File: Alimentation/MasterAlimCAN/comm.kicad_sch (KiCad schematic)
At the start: 17 parts, among them J2 DEBUG, J3 In App Prog, J4 I2C1_5, J5 I2C2_5, J6 CAN1, J7 CAN2, SW1 RESET, SW2 BOOT0, U6 MCP2558FD-xSN

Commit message: Init placement for MasterAlimCAN
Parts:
- J3: footprint Connector_JST:JST_EH_S2B-EH_1x02_P2.50mm_Horizontal -> Connector_JST:JST_PH_S2B-PH-K_1x02_P2.00mm_Horizontal
- J4, J5, J6, J7: footprint Connector_JST:JST_EH_S4B-EH_1x04_P2.50mm_Horizontal -> Connector_JST:JST_PH_S4B-PH-K_1x04_P2.00mm_Horizontal
- renumbered C16 to C15, C17 to C16, C18 to C17, R11 to R10, R12 to R11, R13 to R12, U6 to U5

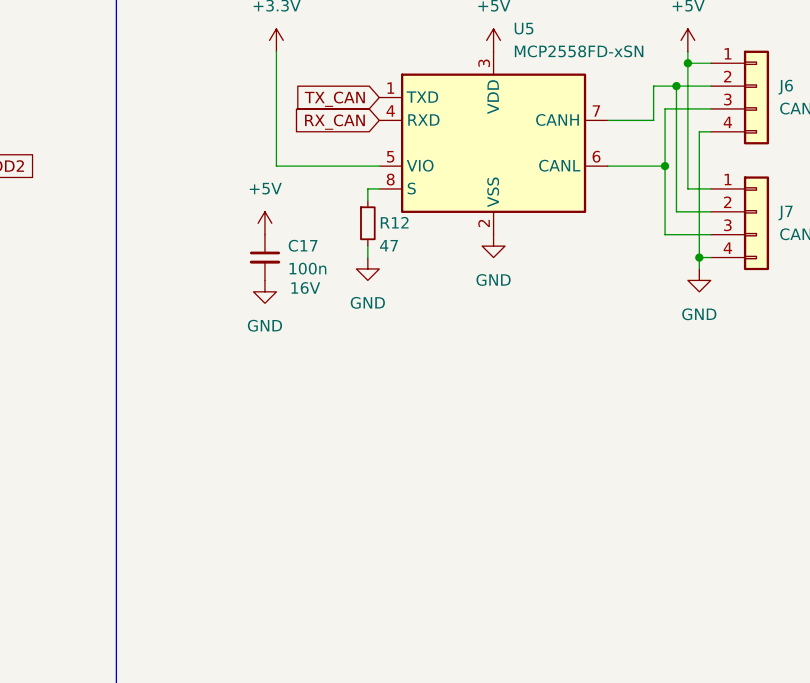
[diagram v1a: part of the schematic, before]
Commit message: New placement for Alim
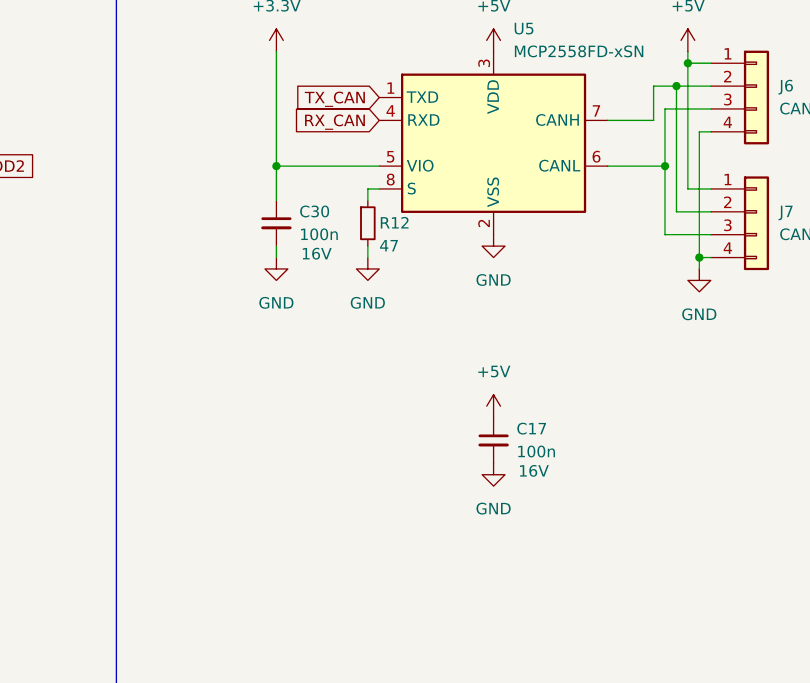
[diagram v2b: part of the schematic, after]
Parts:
- added C30: 100n, Capacitor_SMD:C_0402_1005Metric_Pad0.74x0.62mm_HandSolder, symbol Device:C_Small
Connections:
- net +3.3V: now also C30.1
- net GND: now also C30.2
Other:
- moved on the sheet: C17
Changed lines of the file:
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@@
   (junction (at 85.09 78.74) (diameter 0) (color 0 0 0 0)
+  )
+  (junction (at 182.88 90.17) (diameter 0) (color 0 0 0 0)
   )
   (junction (at 229.87 100.33) (diameter 0) (color 0 0 0 0)
@@
     (stroke (width 0) (type default))
   )
+  (wire (pts (xy 182.88 99.06) (xy 182.88 100.33))
+    (stroke (width 0) (type default))
+  )
   (wire (pts (xy 129.54 111.76) (xy 130.81 111.76))
     (stroke (width 0) (type default))
@@
   )
   (wire (pts (xy 227.33 95.25) (xy 227.33 81.28))
+    (stroke (width 0) (type default))
+  )
+  (wire (pts (xy 182.88 90.17) (xy 182.88 93.98))
     (stroke (width 0) (type default))
   )
@@
     )
   )
-  (symbol (lib_id "power:GND") (at 181.61 102.87 0) (unit 1)
-    (in_bom yes) (on_board yes) (dnp no) (fields_autoplaced)
-    (property "Reference" "#PWR055" (at 181.61 109.22 0)
-      (effects (font (size 1.27 1.27)) hide)
-    )
-    (property "Value" "GND" (at 181.61 107.95 0)
-      (effects (font (size 1.27 1.27)))
-    )
-    (property "Footprint" "" (at 181.61 102.87 0)
-      (effects (font (size 1.27 1.27)) hide)
-    )
-    (property "Datasheet" "" (at 181.61 102.87 0)
+  (symbol (lib_id "power:GND") (at 207.01 123.19 0) (unit 1)
+    (in_bom yes) (on_board yes) (dnp no) (fields_autoplaced)
+    (property "Reference" "#PWR055" (at 207.01 129.54 0)
+      (effects (font (size 1.27 1.27)) hide)
+    )
+    (property "Value" "GND" (at 207.01 128.27 0)
+      (effects (font (size 1.27 1.27)))
+    )
+    (property "Footprint" "" (at 207.01 123.19 0)
+      (effects (font (size 1.27 1.27)) hide)
+    )
+    (property "Datasheet" "" (at 207.01 123.19 0)
       (effects (font (size 1.27 1.27)) hide)
     )
@@
     )
   )
-  (symbol (lib_id "power:+5V") (at 181.61 97.79 0) (unit 1)
-    (in_bom yes) (on_board yes) (dnp no) (fields_autoplaced)
-    (property "Reference" "#PWR054" (at 181.61 101.6 0)
-      (effects (font (size 1.27 1.27)) hide)
-    )
-    (property "Value" "+5V" (at 181.61 92.71 0)
-      (effects (font (size 1.27 1.27)))
-    )
-    (property "Footprint" "" (at 181.61 97.79 0)
-      (effects (font (size 1.27 1.27)) hide)
-    )
-    (property "Datasheet" "" (at 181.61 97.79 0)
+  (symbol (lib_id "power:+5V") (at 207.01 118.11 0) (unit 1)
+    (in_bom yes) (on_board yes) (dnp no) (fields_autoplaced)
+    (property "Reference" "#PWR054" (at 207.01 121.92 0)
+      (effects (font (size 1.27 1.27)) hide)
+    )
+    (property "Value" "+5V" (at 207.01 113.03 0)
+      (effects (font (size 1.27 1.27)))
+    )
+    (property "Footprint" "" (at 207.01 118.11 0)
+      (effects (font (size 1.27 1.27)) hide)
+    )
+    (property "Datasheet" "" (at 207.01 118.11 0)
       (effects (font (size 1.27 1.27)) hide)
     )
@@
     )
   )
+  (symbol (lib_id "Device:C_Small") (at 182.88 96.52 0) (unit 1)
+    (in_bom yes) (on_board yes) (dnp no)
+    (property "Reference" "C30" (at 185.42 95.2563 0)
+      (effects (font (size 1.27 1.27)) (justify left))
+    )
+    (property "Value" "100n" (at 185.42 97.7963 0)
+      (effects (font (size 1.27 1.27)) (justify left))
+    )
+    (property "Footprint" "Capacitor_SMD:C_0402_1005Metric_Pad0.74x0.62mm_HandSolder" (at 182.88 96.52 0)
+      (effects (font (size 1.27 1.27)) hide)
+    )
+    (property "Datasheet" "~" (at 182.88 96.52 0)
+      (effects (font (size 1.27 1.27)) hide)
+    )
+    (property "JLCPCB BOM" "" (at 182.88 96.52 0)
+      (effects (font (size 1.27 1.27)) hide)
+    )
+    (property "LCSC Part" "C1525" (at 182.88 96.52 0)
+      (effects (font (size 1.27 1.27)) hide)
+    )
+    (property "Tension" "16V" (at 187.325 99.949 0)
+      (effects (font (size 1.27 1.27)))
+    )
+    (pin "1")
+    (pin "2")
+    (instances
+      (project "MasterAlimCAN"
+        (path "/c83bc042-587c-48f9-abdb-41233c8ec938/a4b1e0da-5816-453f-b06d-61ca2c30c9c0"
+          (reference "C30") (unit 1)
+        )
+      )
+    )
+  )
+  (symbol (lib_id "power:GND") (at 182.88 100.33 0) (unit 1)
+    (in_bom yes) (on_board yes) (dnp no) (fields_autoplaced)
+    (property "Reference" "#PWR0102" (at 182.88 106.68 0)
+      (effects (font (size 1.27 1.27)) hide)
+    )
+    (property "Value" "GND" (at 182.88 105.41 0)
+      (effects (font (size 1.27 1.27)))
+    )
+    (property "Footprint" "" (at 182.88 100.33 0)
+      (effects (font (size 1.27 1.27)) hide)
+    )
+    (property "Datasheet" "" (at 182.88 100.33 0)
+      (effects (font (size 1.27 1.27)) hide)
+    )
+    (pin "1")
+    (instances
+      (project "MasterAlimCAN"
+        (path "/c83bc042-587c-48f9-abdb-41233c8ec938/a4b1e0da-5816-453f-b06d-61ca2c30c9c0"
+          (reference "#PWR0102") (unit 1)
+        )
+      )
+    )
+  )
   (symbol (lib_id "power:GND") (at 229.87 101.6 0) (unit 1)
     (in_bom yes) (on_board yes) (dnp no) (fields_autoplaced)
@@
     )
   )
-  (symbol (lib_id "Device:C_Small") (at 181.61 100.33 0) (unit 1)
+  (symbol (lib_id "Device:C_Small") (at 207.01 120.65 0) (unit 1)
     (in_bom yes) (on_board yes) (dnp no)
-    (property "Reference" "C17" (at 184.15 99.0663 0)
-      (effects (font (size 1.27 1.27)) (justify left))
-    )
-    (property "Value" "100n" (at 184.15 101.6063 0)
-      (effects (font (size 1.27 1.27)) (justify left))
-    )
-    (property "Footprint" "Capacitor_SMD:C_0402_1005Metric_Pad0.74x0.62mm_HandSolder" (at 181.61 100.33 0)
-      (effects (font (size 1.27 1.27)) hide)
-    )
-    (property "Datasheet" "~" (at 181.61 100.33 0)
-      (effects (font (size 1.27 1.27)) hide)
-    )
-    (property "JLCPCB BOM" "" (at 181.61 100.33 0)
-      (effects (font (size 1.27 1.27)) hide)
-    )
-    (property "LCSC Part" "C1525" (at 181.61 100.33 0)
-      (effects (font (size 1.27 1.27)) hide)
-    )
-    (property "Tension" "16V" (at 186.055 103.759 0)
-      (effects (font (size 1.27 1.27)))
-    )
+    (property "Reference" "C17" (at 209.55 119.3863 0)
+      (effects (font (size 1.27 1.27)) (justify left))
+    )
+    (property "Value" "100n" (at 209.55 121.9263 0)
+      (effects (font (size 1.27 1.27)) (justify left))
+    )
+    (property "Footprint" "Capacitor_SMD:C_0402_1005Metric_Pad0.74x0.62mm_HandSolder" (at 207.01 120.65 0)
+      (effects (font (size 1.27 1.27)) hide)
+    )
+    (property "Datasheet" "~" (at 207.01 120.65 0)
+      (effects (font (size 1.27 1.27)) hide)
+    )
+    (property "JLCPCB BOM" "" (at 207.01 120.65 0)
+      (effects (font (size 1.27 1.27)) hide)
+    )
+    (property "LCSC Part" "C1525" (at 207.01 120.65 0)
+      (effects (font (size 1.27 1.27)) hide)
+    )
+    (property "Tension" "16V" (at 211.455 124.079 0)
+      (effects (font (size 1.27 1.27)))
+    )

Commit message: Finish component placement on MasterAlimCAN
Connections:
- net at J6.2 (Pin_2), J7.2 (Pin_2): now also U5.6 (CANL); no longer U5.7 (CANH)
- net at J6.3 (Pin_3), J7.3 (Pin_3): now also U5.7 (CANH); no longer U5.6 (CANL)
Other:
- moved on the sheet: J6, J7
